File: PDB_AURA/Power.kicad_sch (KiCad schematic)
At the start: 18 parts, among them J100 XT30PW-M, Q100 CSD18540Q5B, U100 LM74700

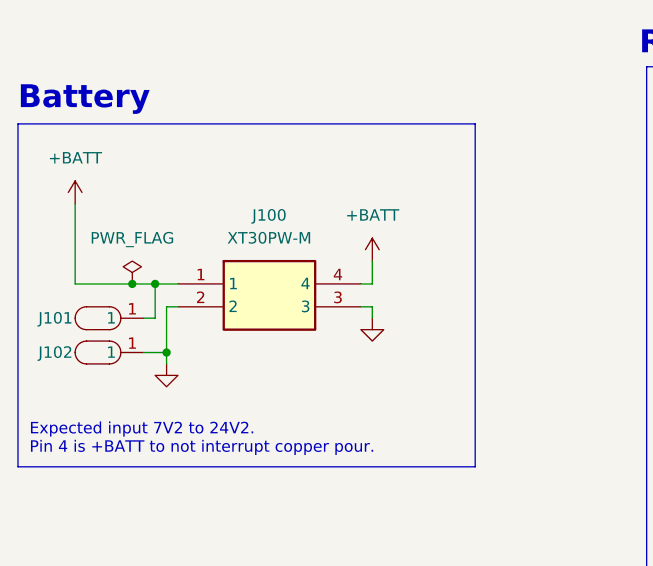
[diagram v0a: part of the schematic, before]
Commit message: Silk Screen Done
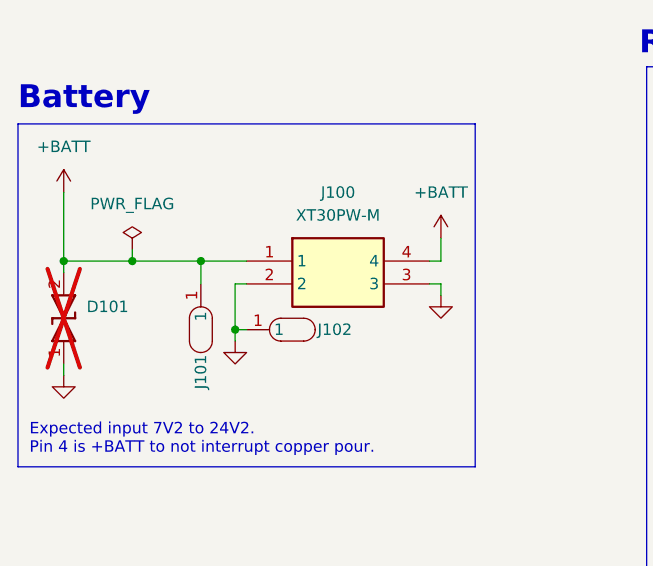
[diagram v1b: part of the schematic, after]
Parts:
- added D101: SMBJ33CA, DIONM5436X244N, symbol SMBJ33CA:SMBJ33CA
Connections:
- net +BATT: now also D101.2
- net GND: now also D101.1
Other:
- moved on the sheet: J100, J101, J102

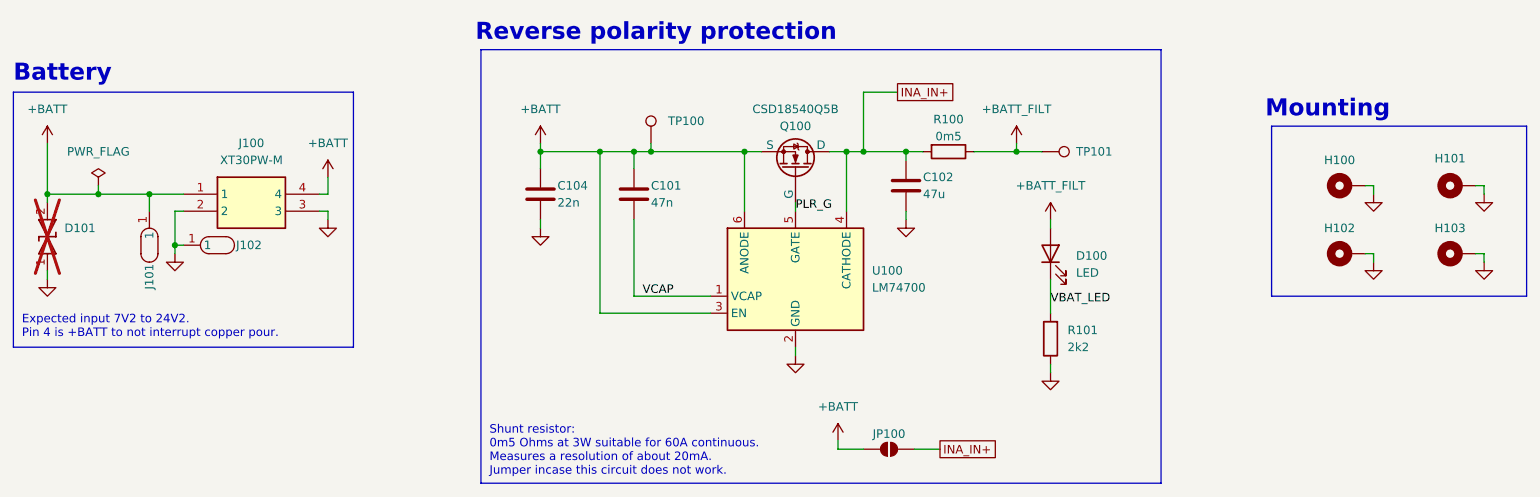
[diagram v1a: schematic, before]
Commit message: Tidied up PDB schematic for documentation.
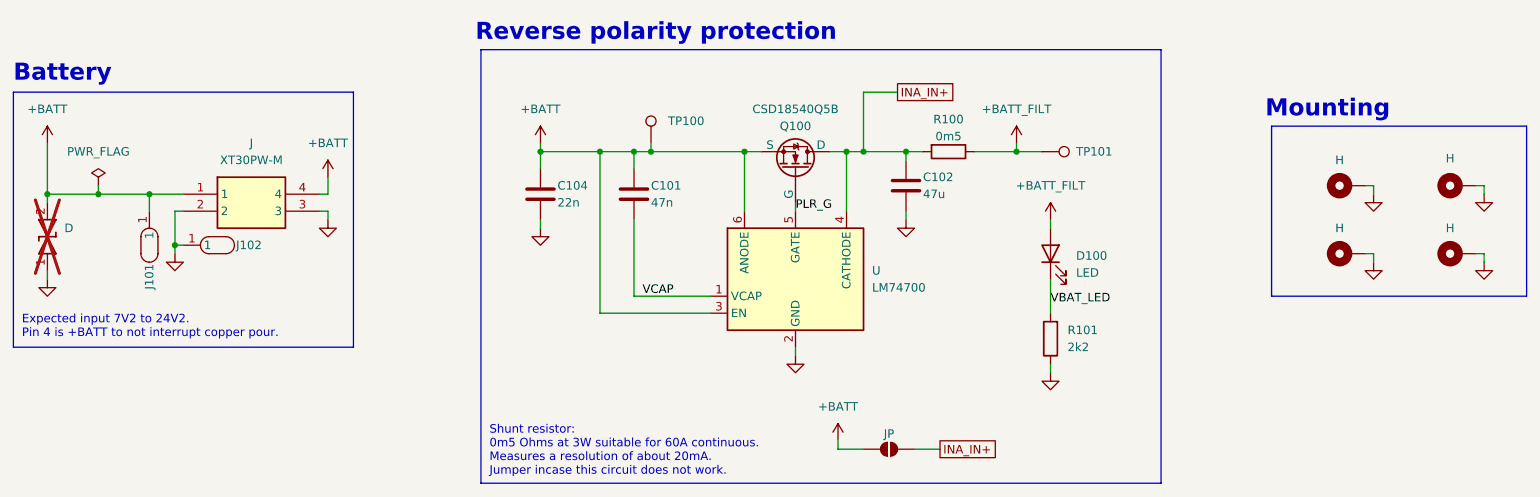
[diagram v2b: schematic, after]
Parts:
- renumbered D101 to D, H100 to H, H102 to H, H101 to H, H103 to H, J100 to J, JP100 to JP, U100 to U
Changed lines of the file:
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@@
 		(dnp no)
 		(fields_autoplaced yes)
-		(property "Reference" "J100"
+		(property "Reference" "J"
 			(at 71.12 76.2 0)
 			(effects
@@
 		(pin "4"
 		)
-		(instances
-			(project ""
-				(path "/c0b09de1-c640-438f-9ef5-dda14a6aac71/c5906580-2f17-4557-899f-eb3151fe9c9e"
-					(reference "J100")
-					(unit 1)
-				)
-			)
-		)
+		(instances)
 	)
 	(symbol
@@
 		(dnp yes)
 		(fields_autoplaced yes)
-		(property "Reference" "D101"
+		(property "Reference" "D"
 			(at 43.18 88.8999 90)
 			(effects
@@
 		(pin "2"
 		)
-		(instances
-			(project ""
-				(path "/c0b09de1-c640-438f-9ef5-dda14a6aac71/c5906580-2f17-4557-899f-eb3151fe9c9e"
-					(reference "D101")
-					(unit 1)
-				)
-			)
-		)
+		(instances)
 	)
 	(symbol
@@
 		(dnp no)
 		(fields_autoplaced yes)
-		(property "Reference" "#PWR055"
+		(property "Reference" "#PWR"
 			(at 82.55 93.98 0)
 			(effects
@@
 		(pin "1"
 		)
-		(instances
-			(project "Summer2025"
-				(path "/c0b09de1-c640-438f-9ef5-dda14a6aac71/c5906580-2f17-4557-899f-eb3151fe9c9e"
-					(reference "#PWR055")
-					(unit 1)
-				)
-			)
-		)
+		(instances)
 	)
 	(symbol
@@
 		(on_board yes)
 		(dnp no)
-		(property "Reference" "H100"
+		(property "Reference" "H"
 			(at 233.68 78.74 90)
 			(effects
@@
 		(pin "1"
 		)
-		(instances
-			(project ""
-				(path "/c0b09de1-c640-438f-9ef5-dda14a6aac71/c5906580-2f17-4557-899f-eb3151fe9c9e"
-					(reference "H100")
-					(unit 1)
-				)
-			)
-		)
+		(instances)
 	)
 	(symbol
@@
 		(on_board yes)
 		(dnp no)
-		(property "Reference" "H102"
+		(property "Reference" "H"
 			(at 233.68 88.9 90)
 			(effects
@@
 		(pin "1"
 		)
-		(instances
-			(project "Summer2025"
-				(path "/c0b09de1-c640-438f-9ef5-dda14a6aac71/c5906580-2f17-4557-899f-eb3151fe9c9e"
-					(reference "H102")
-					(unit 1)
-				)
-			)
-		)
+		(instances)
 	)
 	(symbol
@@
 		(dnp no)
 		(fields_autoplaced yes)
-		(property "Reference" "U100"
+		(property "Reference" "U"
 			(at 163.83 95.2499 0)
 			(effects
@@
 		(pin "4"
 		)
-		(instances
-			(project ""
-				(path "/c0b09de1-c640-438f-9ef5-dda14a6aac71/c5906580-2f17-4557-899f-eb3151fe9c9e"
-					(reference "U100")
-					(unit 1)
-				)
-			)
-		)
+		(instances)
 	)
 	(symbol
@@
 		(dnp no)
 		(fields_autoplaced yes)
-		(property "Reference" "#PWR054"
+		(property "Reference" "#PWR"
 			(at 59.69 99.06 0)
 			(effects
@@
 		(pin "1"
 		)
-		(instances
-			(project "Summer2025"
-				(path "/c0b09de1-c640-438f-9ef5-dda14a6aac71/c5906580-2f17-4557-899f-eb3151fe9c9e"
-					(reference "#PWR054")
-					(unit 1)
-				)
-			)
-		)
+		(instances)
 	)
 	(symbol
@@
 		(on_board yes)
 		(dnp no)
-		(property "Reference" "H101"
+		(property "Reference" "H"
 			(at 250.19 78.486 90)
 			(effects
@@
 		(pin "1"
 		)
-		(instances
-			(project "Summer2025"
-				(path "/c0b09de1-c640-438f-9ef5-dda14a6aac71/c5906580-2f17-4557-899f-eb3151fe9c9e"
-					(reference "H101")
-					(unit 1)
-				)
-			)
-		)
+		(instances)
 	)
 	(symbol
@@
 		(dnp no)
 		(fields_autoplaced yes)
-		(property "Reference" "#FLG05"
+		(property "Reference" "#FLG"
 			(at 48.26 80.645 0)
 			(effects
@@
 		(pin "1"
 		)
-		(instances
-			(project "Summer2025"
-				(path "/c0b09de1-c640-438f-9ef5-dda14a6aac71/c5906580-2f17-4557-899f-eb3151fe9c9e"
-					(reference "#FLG05")
-					(unit 1)
-				)
-			)
-		)
+		(instances)
 	)
 	(symbol
@@
 		(on_board yes)
 		(dnp no)
-		(property "Reference" "JP100"
+		(property "Reference" "JP"
 			(at 166.37 119.634 0)
 			(effects
@@
 		(pin "2"
 		)
-		(instances
-			(project ""
-				(path "/c0b09de1-c640-438f-9ef5-dda14a6aac71/c5906580-2f17-4557-899f-eb3151fe9c9e"
-					(reference "JP100")
-					(unit 1)
-				)
-			)
-		)
+		(instances)
 	)
 	(symbol
@@
 		(on_board yes)
 		(dnp no)
-		(property "Reference" "H103"
+		(property "Reference" "H"
 			(at 250.19 88.9 90)
 			(effects
@@
 		(pin "1"
 		)
-		(instances
-			(project "Summer2025"
-				(path "/c0b09de1-c640-438f-9ef5-dda14a6aac71/c5906580-2f17-4557-899f-eb3151fe9c9e"
-					(reference "H103")
-					(unit 1)
-				)
-			)
-		)
+		(instances)
 	)
 	(symbol
@@
 		(dnp no)
 		(fields_autoplaced yes)
-		(property "Reference" "#PWR053"
+		(property "Reference" "#PWR"
 			(at 40.64 80.01 0)
 			(effects
@@
 		(pin "1"
 		)
-		(instances
-			(project "Summer2025"
-				(path "/c0b09de1-c640-438f-9ef5-dda14a6aac71/c5906580-2f17-4557-899f-eb3151fe9c9e"
-					(reference "#PWR053")
-					(unit 1)
-				)
-			)
-		)
+		(instances)
 	)
 )
